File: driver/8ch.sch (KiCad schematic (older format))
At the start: 48 parts, among them Q301 DMN60H080DS-7, Q302 DMN60H080DS-7, Q303 PBHV9050T,215, Q304 DMN60H080DS-7, Q305 PBHV9050T,215, Q306 DMN60H080DS-7, Q307 DMN60H080DS-7, Q308 DMN60H080DS-7, Q309 PBHV9050T,215, Q310 DMN60H080DS-7, Q311 PBHV9050T,215, Q312 DMN60H080DS-7, Q313 DMN60H080DS-7, Q314 DMN60H080DS-7, Q315 PBHV9050T,215, Q316 DMN60H080DS-7, Q317 PBHV9050T,215, Q318 DMN60H080DS-7, Q319 DMN60H080DS-7, Q320 DMN60H080DS-7, Q321 PBHV9050T,215, Q322 DMN60H080DS-7, Q323 PBHV9050T,215, Q324 DMN60H080DS-7

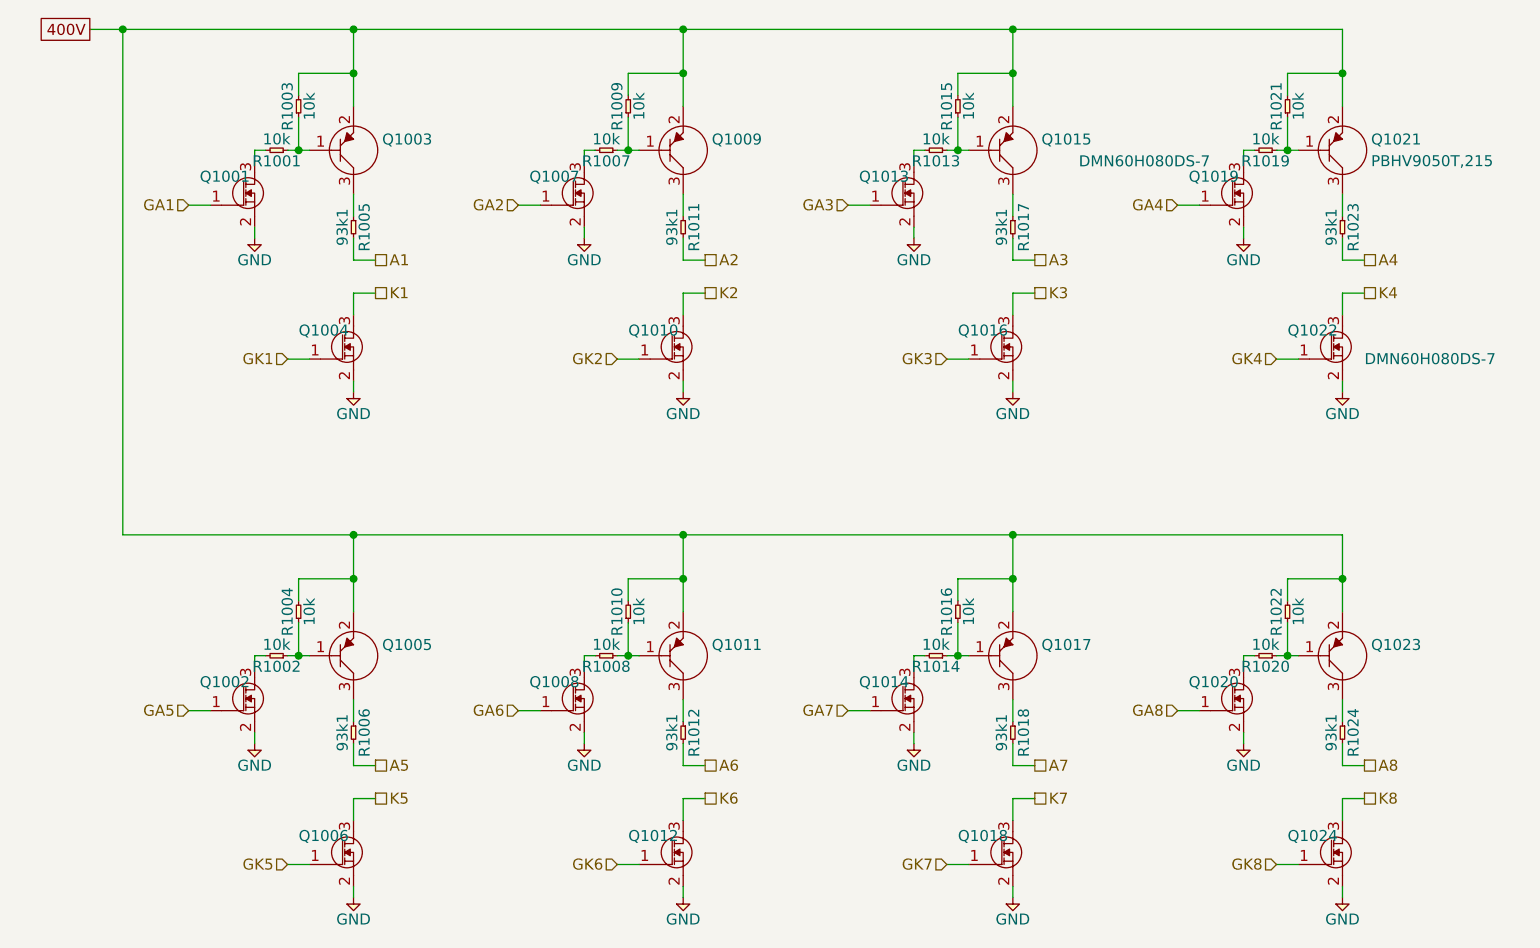
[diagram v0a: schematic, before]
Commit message: Finish sch, start PCB
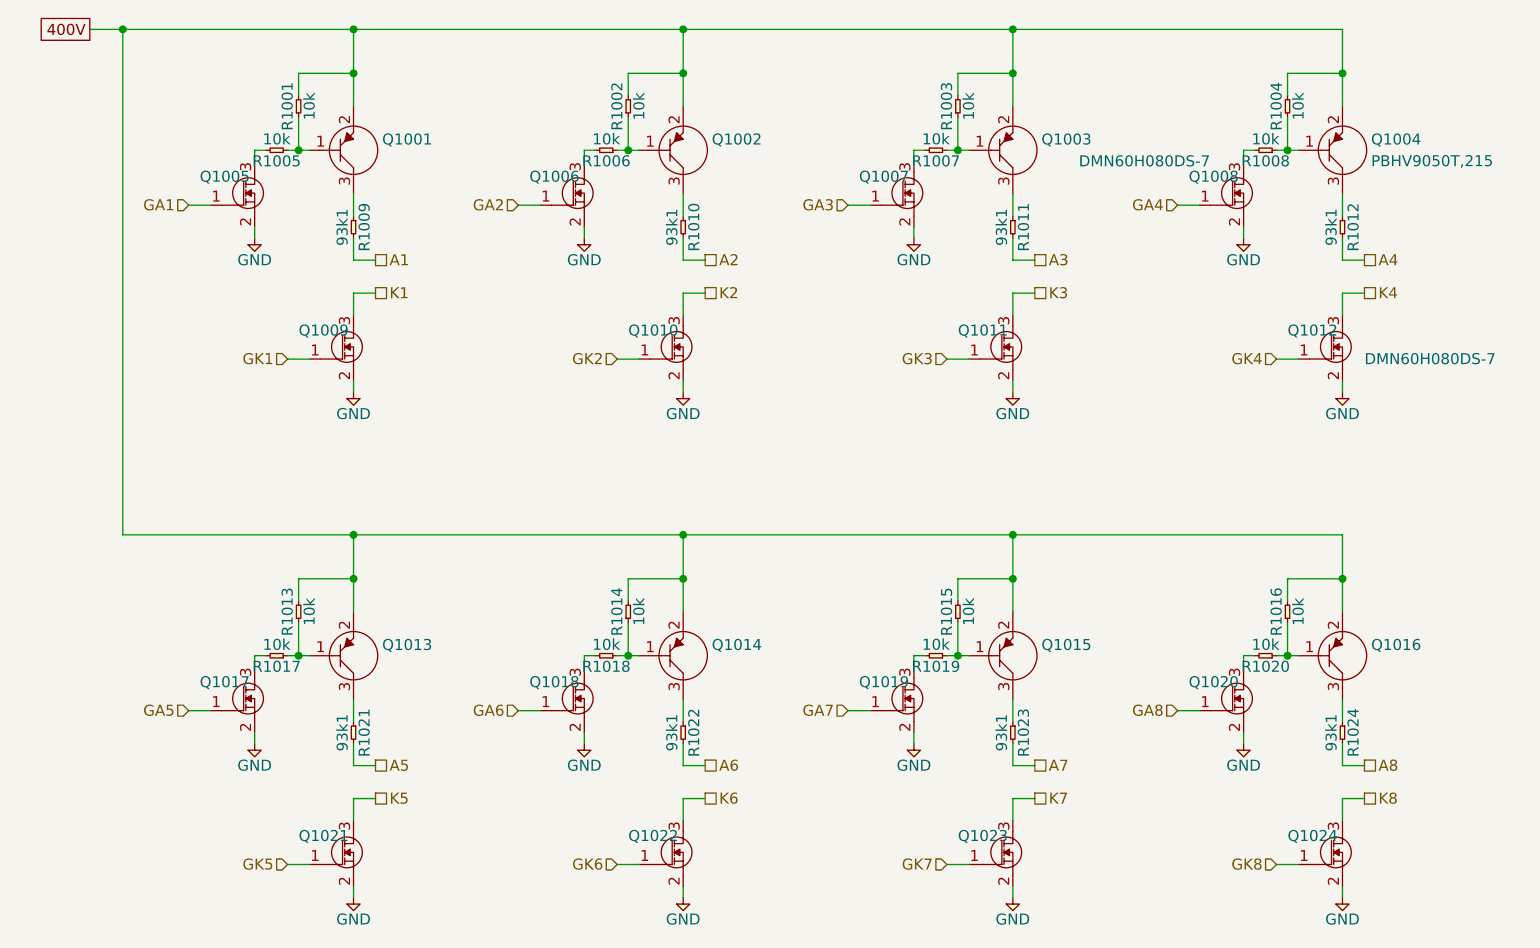
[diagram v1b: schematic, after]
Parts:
- renumbered Q303 to Q301, Q309 to Q302, Q315 to Q303, Q321 to Q304, Q301 to Q305, Q307 to Q306, Q313 to Q307, Q319 to Q308, Q304 to Q309, Q316 to Q311, Q322 to Q312, Q305 to Q313, Q311 to Q314, Q317 to Q315, Q323 to Q316, Q302 to Q317, Q308 to Q318, Q314 to Q319, Q306 to Q321, Q312 to Q322, Q318 to Q323, R303 to R301, R309 to R302, R315 to R303, R321 to R304, R301 to R305, R307 to R306, R313 to R307, R319 to R308, R305 to R309, R311 to R310, R317 to R311, R323 to R312, R304 to R313, R310 to R314, R316 to R315, R322 to R316, R302 to R317, R308 to R318, R314 to R319, R306 to R321, R312 to R322, R318 to R323

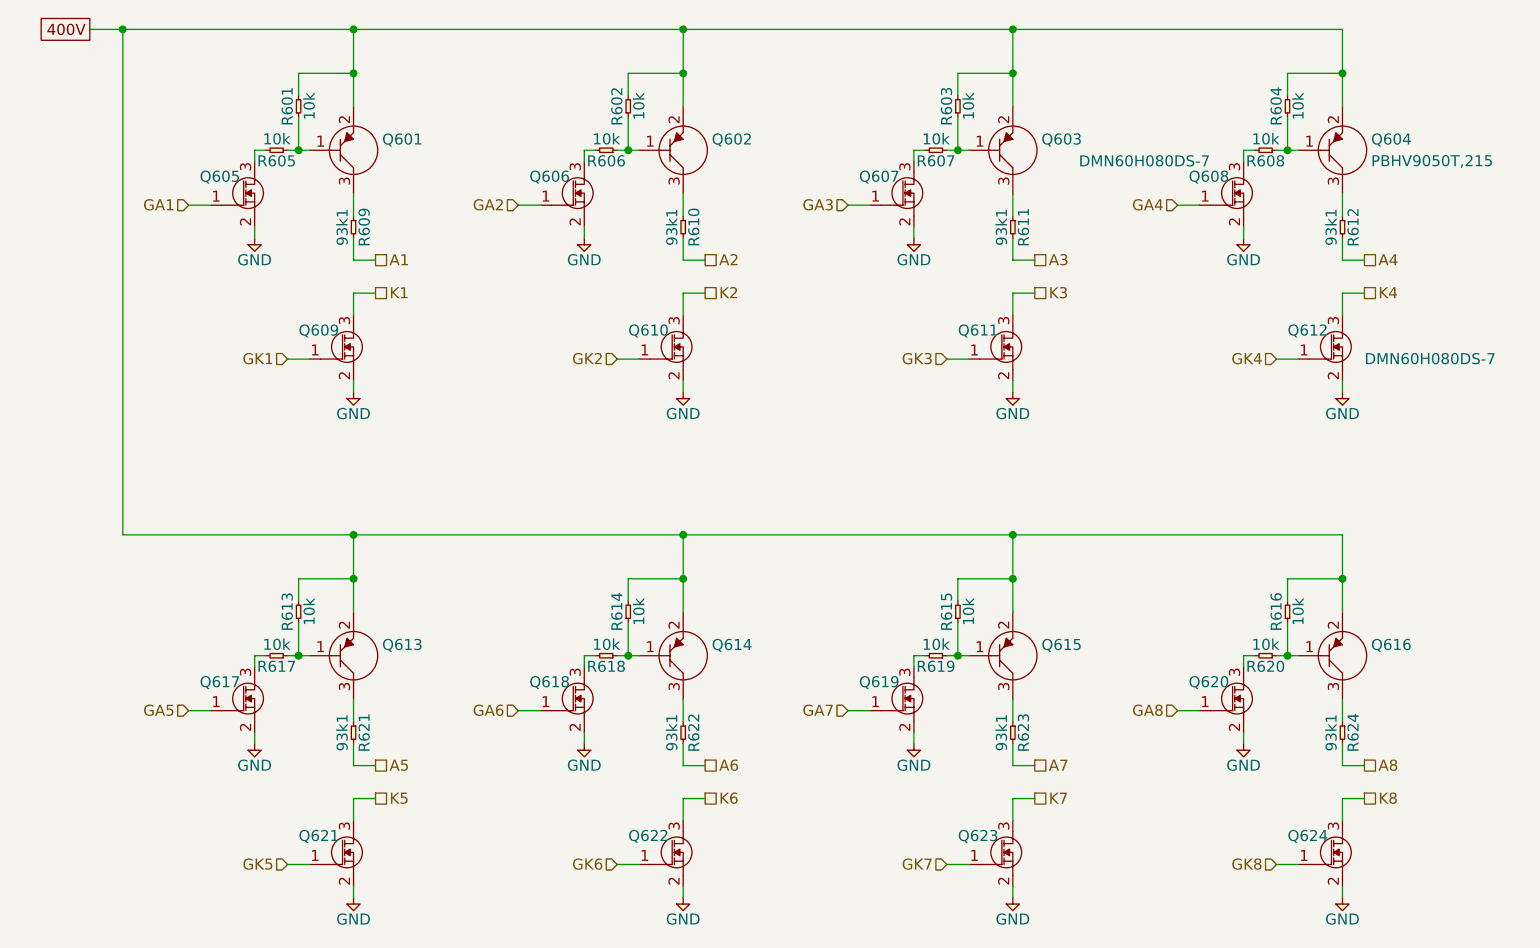
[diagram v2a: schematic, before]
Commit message: Start work on 32ch board
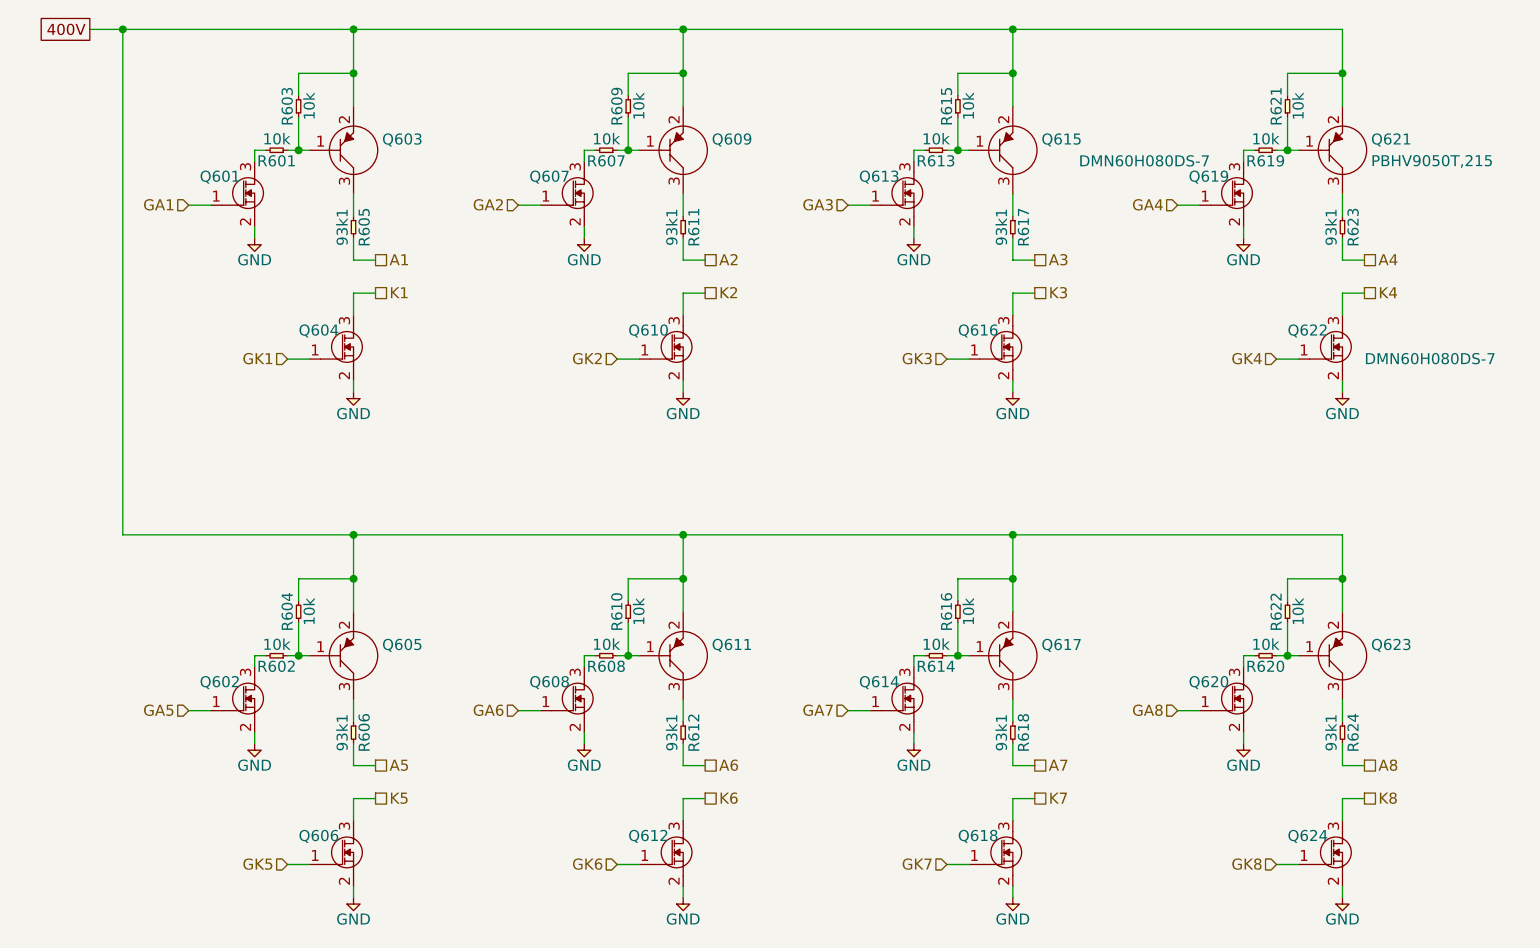
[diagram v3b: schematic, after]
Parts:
- renumbered Q305 to Q301, Q317 to Q302, Q301 to Q303, Q309 to Q304, Q313 to Q305, Q321 to Q306, Q306 to Q307, Q318 to Q308, Q302 to Q309, Q314 to Q311, Q322 to Q312, Q307 to Q313, Q319 to Q314, Q303 to Q315, Q311 to Q316, Q315 to Q317, Q323 to Q318, Q308 to Q319, Q304 to Q321, Q312 to Q322, Q316 to Q323, R305 to R301, R317 to R302, R301 to R303, R313 to R304, R309 to R305, R321 to R306, R306 to R307, R318 to R308, R302 to R309, R314 to R310, R310 to R311, R322 to R312, R307 to R313, R319 to R314, R303 to R315, R315 to R316, R311 to R317, R323 to R318, R308 to R319, R304 to R321, R316 to R322, R312 to R323

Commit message: more layout work
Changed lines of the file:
@@
 $Descr A4 11693 8268
 encoding utf-8
-Sheet 4 7
+Sheet 6 7
 Title "IGGie Driver Board"
 Date "2019-09-26"
@@
 Text HLabel 4850 4850 2    50   UnSpc ~ 0
 A6
-Text HLabel 4850 5000 2    50   UnSpc ~ 0
+Text HLabel 4250 2300 2    50   UnSpc ~ 0
 K6
 Text HLabel 4450 5300 0    50   Input ~ 0
@@
 Text HLabel 3350 2550 2    50   UnSpc ~ 0
 A1
+Text HLabel 4850 5000 2    50   UnSpc ~ 0
+K6
 $EndSCHEMATC
